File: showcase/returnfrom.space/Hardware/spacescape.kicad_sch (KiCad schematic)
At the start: 8 parts, among them J4 Conn_02x04_Counter_Clockwise, J5 Conn_01x03_Pin, J6 Conn_01x05_Pin, SW0 SW_SPST, U1 ATtiny1616-M

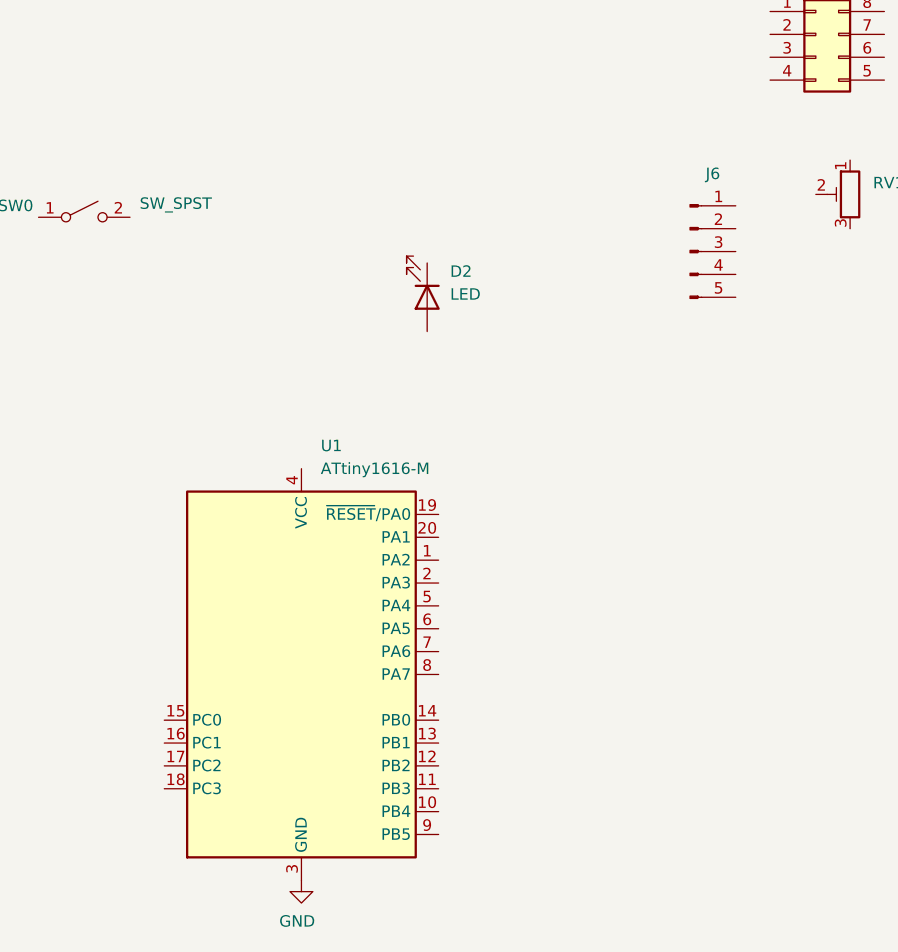
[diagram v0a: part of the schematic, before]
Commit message: added step files
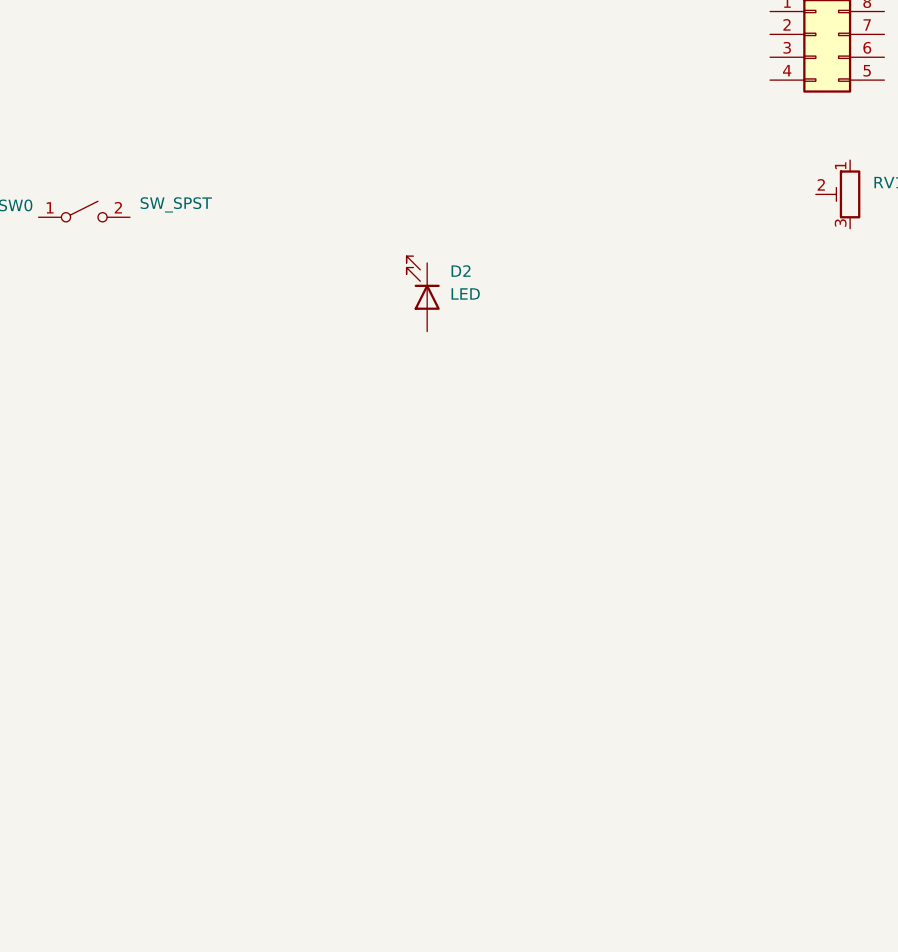
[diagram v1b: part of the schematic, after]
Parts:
- removed J6: Conn_01x05_Pin, Connector_PinHeader_2.54mm:PinHeader_1x05_P2.54mm_Vertical, symbol Connector:Conn_01x05_Pin
- removed U1: ATtiny1616-M, Package_DFN_QFN:VQFN-20-1EP_3x3mm_P0.4mm_EP1.7x1.7mm, symbol MCU_Microchip_ATtiny:ATtiny1616-M

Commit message: updated
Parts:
- removed D1: WS2812B-2020, LED_SMD:LED_WS2812B-2020_PLCC4_2.0x2.0mm, symbol LED:WS2812B-2020
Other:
- removed sheet supply
- moved on the sheet: D2, SW0
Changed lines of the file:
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@@
 	(paper "A4")
-	(symbol
-		(lib_id "power:GND")
-		(at 38.1 104.14 0)
-		(unit 1)
-		(exclude_from_sim no)
-		(in_bom yes)
-		(on_board yes)
-		(dnp no)
-		(property "Reference" "#PWR08"
-			(at 38.1 110.49 0)
-			(effects
-				(font
-					(size 1.27 1.27)
-				)
-				(hide yes)
-			)
-		)
-		(property "Value" "GND"
-			(at 39.624 108.712 0)
-			(effects
-				(font
-					(size 1.27 1.27)
-				)
-				(justify right)
-			)
-		)
-		(property "Footprint" ""
-			(at 38.1 104.14 0)
-			(effects
-				(font
-					(size 1.27 1.27)
-				)
-				(hide yes)
-			)
-		)
-		(property "Datasheet" ""
-			(at 38.1 104.14 0)
-			(effects
-				(font
-					(size 1.27 1.27)
-				)
-				(hide yes)
-			)
-		)
-		(property "Description" "Power symbol creates a global label with name \"GND\" , ground"
-			(at 38.1 104.14 0)
-			(effects
-				(font
-					(size 1.27 1.27)
-				)
-				(hide yes)
-			)
-		)
-		(pin "1"
-		)
-		(instances
-			(project "spacescape"
-				(path "/418a52ba-b136-48f0-a485-149e9dc1363e"
-					(reference "#PWR08")
-					(unit 1)
-				)
-			)
-		)
-	)
 	(symbol
 		(lib_id "Connector:Conn_01x03_Pin")
@@
 	)
 	(symbol
-		(lib_id "LED:WS2812B-2020")
-		(at 38.1 96.52 0)
-		(unit 1)
-		(exclude_from_sim no)
-		(in_bom yes)
-		(on_board yes)
-		(dnp no)
-		(property "Reference" "D1"
-			(at 52.07 90.0998 0)
-			(effects
-				(font
-					(size 1.27 1.27)
-				)
-			)
-		)
-		(property "Value" "WS2812B-2020"
-			(at 52.07 92.71 0)
-			(effects
-				(font
-					(size 1.27 1.27)
-				)
-			)
-		)
-		(property "Footprint" "LED_SMD:LED_WS2812B-2020_PLCC4_2.0x2.0mm"
-			(at 39.37 104.14 0)
-			(effects
-				(font
-					(size 1.27 1.27)
-				)
-				(justify left top)
-				(hide yes)
-			)
-		)
-		(property "Datasheet" "https://cdn-shop.adafruit.com/product-files/4684/4684_WS2812B-2020_V1.3_EN.pdf"
-			(at 40.64 106.045 0)
-			(effects
-				(font
-					(size 1.27 1.27)
-				)
-				(justify left top)
-				(hide yes)
-			)
-		)
-		(property "Description" "C965555"
-			(at 38.1 96.52 0)
-			(effects
-				(font
-					(size 1.27 1.27)
-				)
-				(hide yes)
-			)
-		)
-		(pin "2"
-		)
-		(pin "3"
-		)
-		(pin "1"
-		)
-		(pin "4"
-		)
-		(instances
-			(project ""
-				(path "/418a52ba-b136-48f0-a485-149e9dc1363e"
-					(reference "D1")
-					(unit 1)
-				)
-			)
-		)
-	)
-	(symbol
 		(lib_id "Connector_Generic:Conn_02x04_Counter_Clockwise")
 		(at 149.86 82.55 0)
@@
 	(symbol
 		(lib_id "Switch:SW_SPST")
-		(at 68.58 102.87 0)
+		(at 132.08 118.11 0)
 		(unit 1)
 		(exclude_from_sim no)
@@
 		(dnp no)
 		(property "Reference" "SW0"
-			(at 60.96 101.6 0)
+			(at 124.46 116.84 0)
 			(effects
 				(font
@@
 		)
 		(property "Value" "SW_SPST"
-			(at 78.74 101.346 0)
+			(at 142.24 116.586 0)
 			(effects
 				(font
@@
 		)
 		(property "Footprint" "Button_Switch_THT:SW_PUSH_6mm_H4.3mm"
-			(at 68.58 102.87 0)
+			(at 132.08 118.11 0)
 			(effects
 				(font
@@
 		)
 		(property "Datasheet" ""
-			(at 68.58 102.87 0)
+			(at 132.08 118.11 0)
 			(effects
 				(font
@@
 		)
 		(property "Description" "Single Pole Single Throw (SPST) switch"
-			(at 68.58 102.87 0)
+			(at 132.08 118.11 0)
 			(effects
 				(font
@@
 	(symbol
 		(lib_id "Device:LED")
-		(at 106.68 111.76 270)
+		(at 170.18 127 270)
 		(unit 1)
 		(exclude_from_sim no)
@@
 		(fields_autoplaced yes)
 		(property "Reference" "D2"
-			(at 109.22 108.9024 90)
+			(at 172.72 124.1424 90)
 			(effects
 				(font
@@
 		)
 		(property "Value" "LED"
-			(at 109.22 111.4424 90)
+			(at 172.72 126.6824 90)
 			(effects
 				(font
@@
 		)
 		(property "Footprint" "LED_SMD:LED_0805_2012Metric"
-			(at 106.68 111.76 0)
+			(at 170.18 127 0)
 			(effects
 				(font
@@
 		)
 		(property "Datasheet" "~"
-			(at 106.68 111.76 0)
+			(at 170.18 127 0)
 			(effects
 				(font
@@
 		)
 		(property "Description" "Light emitting diode"
-			(at 106.68 111.76 0)
+			(at 170.18 127 0)
 			(effects
 				(font
@@
 		)
 		(property "Sim.Pins" "1=K 2=A"
-			(at 106.68 111.76 0)
+			(at 170.18 127 0)
 			(effects
 				(font
@@
 				)
 			)
-		)
-	)
-	(sheet
-		(at 210.82 102.87)
-		(size 20.32 8.89)
-		(exclude_from_sim no)
-		(in_bom yes)
-		(on_board yes)
-		(dnp no)
-		(fields_autoplaced yes)
-		(stroke
-			(width 0.1524)
-			(type solid)
-		)
-		(fill
-			(color 0 0 0 0.0000)
-		)
-		(property "Sheetname" "supply"
-			(at 210.82 102.1584 0)
-			(effects
-				(font
-					(size 1.27 1.27)
-				)
-				(justify left bottom)
-			)
-		)
-		(property "Sheetfile" "supply.kicad_sch"
-			(at 210.82 112.3446 0)
-			(effects
-				(font
-					(size 1.27 1.27)
-				)
-				(justify left top)
-			)
-		)
-		(instances
-			(project "spacescape"
-				(path "/418a52ba-b136-48f0-a485-149e9dc1363e"
-					(page "6")
-				)
-			)

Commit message: updated
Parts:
- removed D2: LED, LED_SMD:LED_0805_2012Metric, symbol Device:LED
- removed J4: Conn_02x04_Counter_Clockwise, Package_DIP:DIP-8_W7.62mm, symbol Connector_Generic:Conn_02x04_Counter_Clockwise
- removed J5: Conn_01x03_Pin, Connector_PinHeader_2.54mm:PinHeader_1x03_P2.54mm_Vertical, symbol Connector:Conn_01x03_Pin
- removed RV1: R_Potentiometer_Trim, Potentiometer_SMD:Potentiometer_Bourns_TC33X_Vertical, symbol Device:R_Potentiometer_Trim
- removed SW0: SW_SPST, Button_Switch_THT:SW_PUSH_6mm_H4.3mm, symbol Switch:SW_SPST
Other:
- added sheet d-pad (d-pad.kicad_sch)

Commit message: panelizing...
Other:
- removed sheet comms
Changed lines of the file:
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@@
 	(paper "A4")
 	(sheet
-		(at 96.52 59.69)
+		(at 64.77 99.06)
 		(size 25.4 11.43)
 		(exclude_from_sim no)
@@
 		)
 		(property "Sheetname" "d-pad"
-			(at 96.52 58.9784 0)
+			(at 64.77 98.3484 0)
 			(effects
 				(font
@@
 		)
 		(property "Sheetfile" "d-pad.kicad_sch"
-			(at 96.52 71.7046 0)
+			(at 64.77 111.0746 0)
 			(effects
 				(font
@@
 				)
 			)
-		)
-	)
-	(sheet
-		(at 64.77 99.06)
-		(size 25.4 11.43)
-		(exclude_from_sim no)
-		(in_bom yes)
-		(on_board yes)
-		(dnp no)
-		(fields_autoplaced yes)
-		(stroke
-			(width 0.1524)
-			(type solid)
-		)
-		(fill
-			(color 0 0 0 0.0000)
-		)
-		(property "Sheetname" "comms"
-			(at 64.77 98.3484 0)
-			(effects
-				(font
-					(size 1.27 1.27)
-				)
-				(justify left bottom)
-			)
-		)
-		(property "Sheetfile" "comms.kicad_sch"
-			(at 64.77 111.0746 0)
-			(effects
-				(font
-					(size 1.27 1.27)
-				)
-				(justify left top)
-			)
-		)
-		(instances
-			(project "spacescape"
-				(path "/418a52ba-b136-48f0-a485-149e9dc1363e"
-					(page "7")
-				)
-			)
